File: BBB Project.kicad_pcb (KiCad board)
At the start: 2 copper layers, 14.6 x 20.6 mm, 5 parts, among them J1 Conn_02x04_Odd_Even, J2 Conn_01x02_Female, SW1 SW_Push, U1 MAX6816

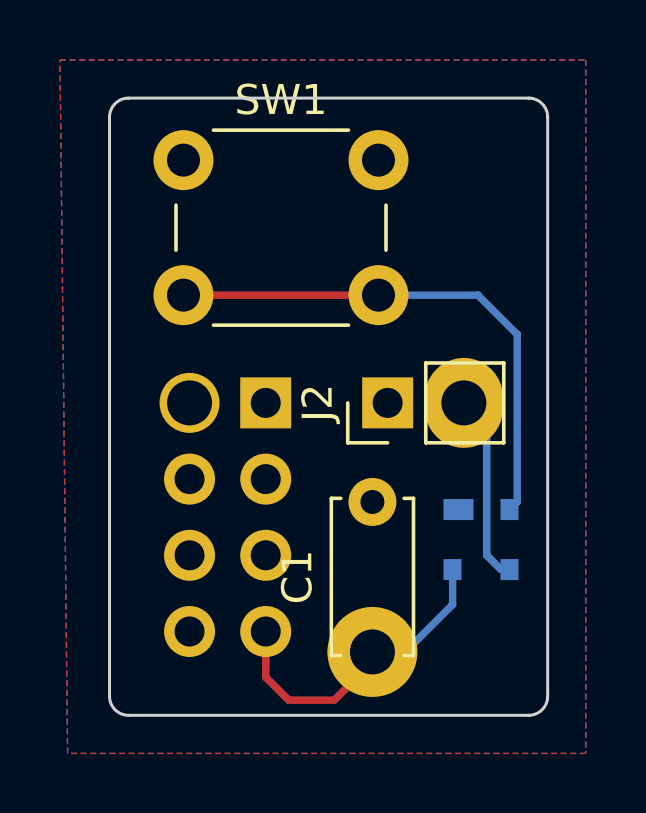
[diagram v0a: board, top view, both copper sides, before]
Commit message: Fixed voltage and verified board
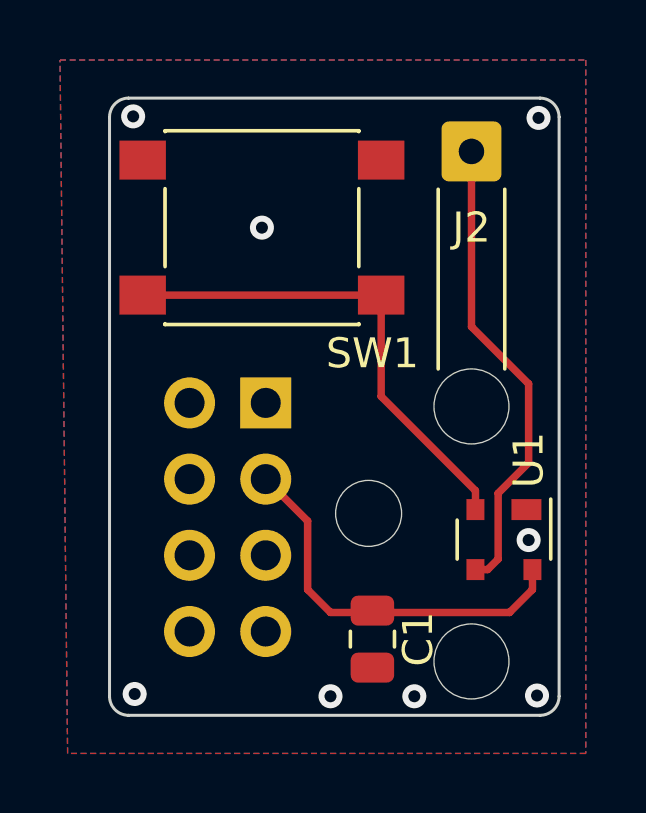
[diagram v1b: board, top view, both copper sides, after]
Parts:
- added REF**: MountingHole_2.2mm_M2, MountingHole:MountingHole_2.2mm_M2, F.Cu at (152.8, 67.9)
- C1: footprint Capacitor_THT:C_Disc_D5.0mm_W2.5mm_P5.00mm -> Capacitor_SMD:C_0805_2012Metric
- J2: value Conn_01x02_Female -> Conn_01x01_Pin; footprint Connector_PinHeader_2.54mm:PinHeader_1x02_P2.54mm_Vertical -> Connector_Wire:SolderWire-0.25sqmm_1x01_D0.65mm_OD2mm_Relief2x
- SW1: footprint Button_Switch_THT:SW_PUSH_6mm -> Button_Switch_SMD:SW_Push_1P1T_NO_6x6mm_H9.5mm
- U1: moved to F.Cu
- moved J2 8.84 mm to (156.2, 55.9), turned to 0 degrees
- moved SW1 3.45 mm to (149.2, 58.4)
- moved U1 0.76 mm to (157.3, 68.8)
- moved C1 0.43 mm to (152.9, 72.1), turned to -90 degrees
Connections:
- net Net-(SW1-Pad2) renamed /btn_raw
- C1 pad 1: Net-(J1-Pad7) -> +3V3
- J1 pad 1: unconnected-(J1-Pad1) -> GND
- J1 pad 3: unconnected-(J1-Pad3) -> +3V3
- J1 pad 7: Net-(J1-Pad7) -> unconnected-(J1-Pin_7-Pad7)
- J2 pad 1: GND -> /btn_out
- U1 pad 3: Net-(J2-Pad2) -> /btn_out
- U1 pad 4: Net-(J1-Pad7) -> +3V3
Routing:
- net /btn_out: track 0.00 -> 15.7 mm
- net +3V3: track 0.00 -> 13.1 mm
- net Net-(J1-Pad7): track 10.8 -> 0.00 mm
- net Net-(J2-Pad2): track 6.35 -> 0.00 mm
- net /btn_raw: track 17.6 -> 16.4 mm
- net GND: track 0.41 -> 0.00 mm, vias 0 -> 8
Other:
- board size 14.6 x 20.6 mm -> 15 x 20.6 mm
